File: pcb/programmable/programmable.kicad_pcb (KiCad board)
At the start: 2 copper layers, 88.6 x 167.9 mm, 91 parts, among them J1 AudioJack3_Ground, U1 Raspberry_Pi_Pico

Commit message: numerical done
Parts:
- R23, R24: moved to B.Cu

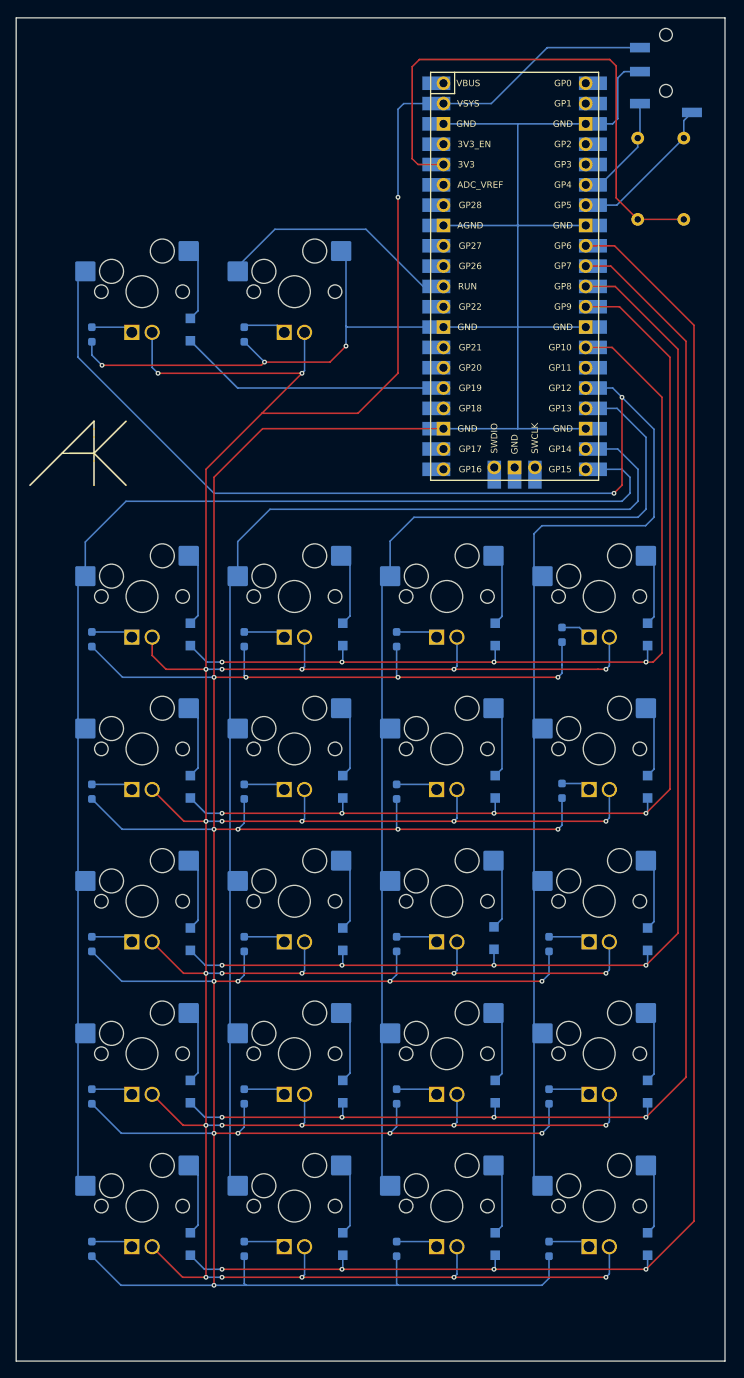
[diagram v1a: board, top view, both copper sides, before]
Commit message: added copper zone fills
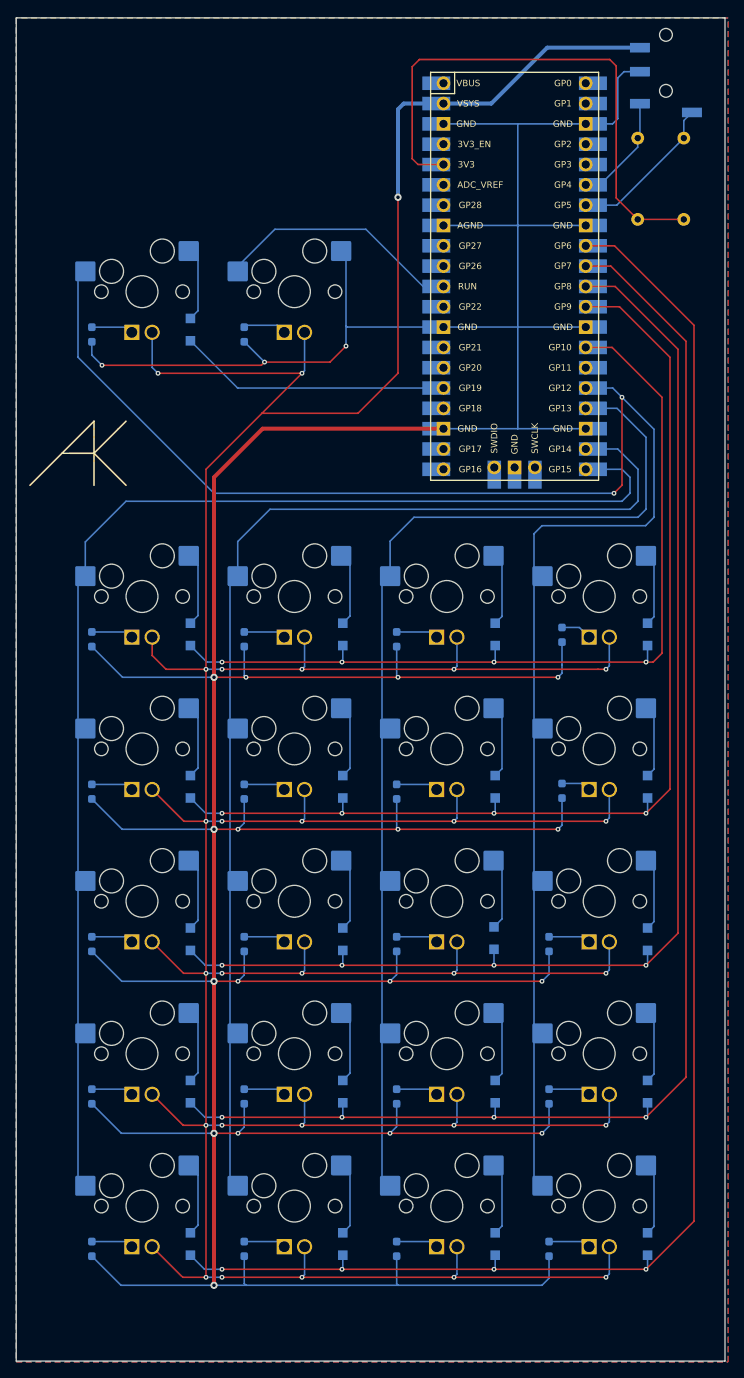
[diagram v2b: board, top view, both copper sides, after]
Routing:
- added copper zone on F.Cu, net +5V
- added copper zone on B.Cu, net GND
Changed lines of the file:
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@@
 			(pinfunction "A")
 			(pintype "passive")
+			(zone_connect 2)
 		)
 	)
@@
 			(pinfunction "VSYS")
 			(pintype "power_in")
+			(zone_connect 2)
 		)
 		(pad "39" smd rect
@@
 	(via
 		(at 91.0525 52.6796)
-		(size 0.6)
-		(drill 0.3)
+		(size 0.9)
+		(drill 0.45)
 		(layers "F.Cu" "B.Cu")
 		(net 47)
@@
 		(start 121.2975 33.9746)
 		(end 109.7075 33.9746)
-		(width 0.2)
+		(width 0.5)
 		(layer "B.Cu")
 		(net 47)
@@
 		(start 109.7075 33.9746)
 		(end 102.7175 40.9646)
-		(width 0.2)
+		(width 0.5)
 		(layer "B.Cu")
 		(net 47)
@@
 		(start 96.7375 40.9646)
 		(end 91.7675 40.9646)
-		(width 0.2)
+		(width 0.5)
 		(layer "B.Cu")
 		(net 47)
@@
 		(start 91.7675 40.9646)
 		(end 91.0525 41.6796)
-		(width 0.2)
+		(width 0.5)
 		(layer "B.Cu")
 		(net 47)
@@
 		(start 91.0525 41.6796)
 		(end 91.0525 52.6796)
-		(width 0.2)
+		(width 0.5)
 		(layer "B.Cu")
 		(net 47)
@@
 		(start 102.7175 40.9646)
 		(end 96.7375 40.9646)
-		(width 0.2)
+		(width 0.5)
 		(layer "B.Cu")
 		(net 47)
@@
 		(start 68.0525 131.6796)
 		(end 68.0525 150.6796)
-		(width 0.2)
+		(width 0.5)
 		(layer "F.Cu")
 		(net 69)
@@
 		(start 96.7375 81.6046)
 		(end 74.1275 81.6046)
-		(width 0.2)
+		(width 0.5)
 		(layer "F.Cu")
 		(net 69)
@@
 		(start 68.0525 87.6796)
 		(end 68.0525 112.6796)
-		(width 0.2)
+		(width 0.5)
 		(layer "F.Cu")
 		(net 69)
@@
 		(start 68.0525 150.6796)
 		(end 68.0525 168.6796)
-		(width 0.2)
+		(width 0.5)
 		(layer "F.Cu")
 		(net 69)
@@
 		(start 74.1275 81.6046)
 		(end 68.0525 87.6796)
-		(width 0.2)
+		(width 0.5)
 		(layer "F.Cu")
 		(net 69)
@@
 		(start 68.0525 112.6796)
 		(end 68.0525 131.6796)
-		(width 0.2)
+		(width 0.5)
 		(layer "F.Cu")
 		(net 69)
@@
 		(start 68.0525 188.6796)
 		(end 68.0525 169.6796)
-		(width 0.2)
+		(width 0.5)
 		(layer "F.Cu")
 		(net 69)
@@
 		(start 68.0525 168.6796)
 		(end 68.0525 169.6796)
-		(width 0.2)
+		(width 0.5)
 		(layer "F.Cu")
 		(net 69)
@@
 	(via
 		(at 68.0525 150.6796)
-		(size 0.6)
-		(drill 0.3)
+		(size 0.9)
+		(drill 0.45)
 		(layers "F.Cu" "B.Cu")
 		(net 69)
@@
 	(via
 		(at 68.0525 169.6796)
-		(size 0.6)
-		(drill 0.3)
+		(size 0.9)
+		(drill 0.45)
 		(layers "F.Cu" "B.Cu")
 		(net 69)
@@
 	(via
 		(at 68.0525 188.6796)
-		(size 0.6)
-		(drill 0.3)
+		(size 0.9)
+		(drill 0.45)
 		(layers "F.Cu" "B.Cu")
 		(net 69)
@@
 	(via
 		(at 68.0525 131.6796)
-		(size 0.6)
-		(drill 0.3)
+		(size 0.9)
+		(drill 0.45)
 		(layers "F.Cu" "B.Cu")
 		(net 69)
@@
 	(via
 		(at 68.0525 112.6796)
-		(size 0.6)
-		(drill 0.3)
+		(size 0.9)
+		(drill 0.45)
 		(layers "F.Cu" "B.Cu")
 		(net 69)
@@
 		(net 78)
 	)
+	(zone
+		(net 47)
+		(net_name "+5V")
+		(layer "F.Cu")
+		(hatch edge 0.5)
+		(connect_pads
+			(clearance 0.5)
+		)
+		(min_thickness 0.25)
+		(filled_areas_thickness no)
+		(fill yes
+			(thermal_gap 0.5)
+			(thermal_bridge_width 0.5)
+		)
+		(polygon
+			(pts
+				(xy 43.3275 30.2546) (xy 43.3275 198.2546) (xy 132.3275 198.2546) (xy 132.3275 30.2546)
+			)
+		)
+	)
+	(zone
+		(net 69)
+		(net_name "GND")
+		(layer "B.Cu")
+		(hatch edge 0.5)
+		(priority 1)
+		(connect_pads
+			(clearance 0.5)
+		)
+		(min_thickness 0.25)
+		(filled_areas_thickness no)
+		(fill yes
+			(thermal_gap 0.5)
+			(thermal_bridge_width 0.5)
+		)
+		(polygon
+			(pts
+				(xy 43.3275 30.2546) (xy 43.3275 198.2546) (xy 132.3275 198.2546) (xy 132.3275 30.2546)
+			)
+		)
+	)
 )

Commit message: gerber files
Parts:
- added REF**: MountingHole_2.2mm_M2, MountingHole:MountingHole_2.2mm_M2, F.Cu at (47.3, 34.3)
- added REF**: MountingHole_2.2mm_M2, MountingHole:MountingHole_2.2mm_M2, F.Cu at (88.3, 85.3)
- added REF**: MountingHole_2.2mm_M2, MountingHole:MountingHole_2.2mm_M2, F.Cu at (47.3, 194.3)
- added REF**: MountingHole_2.2mm_M2, MountingHole:MountingHole_2.2mm_M2, F.Cu at (47.3, 131.3)
- added REF**: MountingHole_2.2mm_M2, MountingHole:MountingHole_2.2mm_M2, F.Cu at (128.3, 194.3)
- added REF**: MountingHole_2.2mm_M2, MountingHole:MountingHole_2.2mm_M2, F.Cu at (128.3, 60.3)
